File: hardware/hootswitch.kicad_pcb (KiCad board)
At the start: 2 copper layers, 100 x 88 mm, 127 parts, among them J1 Mini-DIN-4-G, J10 POWSEL, J11 TWI, J12 TWI, J2 Mini-DIN-4-G, J3 Mini-DIN-4-G, J4 Mini-DIN-4-G, J5 Mini-DIN-4-G, J6 Mini-DIN-4-G, J7 Barrel_Jack_MountingPin, J8 EXT_POW, J9 SW1, Q1 MMBT3904, Q10 MMBT3904, Q11 MMBT3904, Q12 MMBT3904, Q13 MMBT3904, Q14 MMBT3904, Q15 MMBT3904, Q16 MMBT3904, Q2 MMBT3904, Q3 MMBT3904, Q4 MMBT3904, Q5 MMBT3904, Q6 MMBT3904, Q7 MMBT3904, Q8 MMBT3904, Q9 MMBT3904, SW1 Switch1, U1 PicoW, U10 LTV-357T, U11 LTV-357T, U2 LM1117-5.0, U3 ADuM1201AR, U4 ADuM1201AR, U5 ADuM1201AR, U6 ADuM1201AR, U7 ADuM1201AR, U8 LTV-357T, U9 LTV-357T

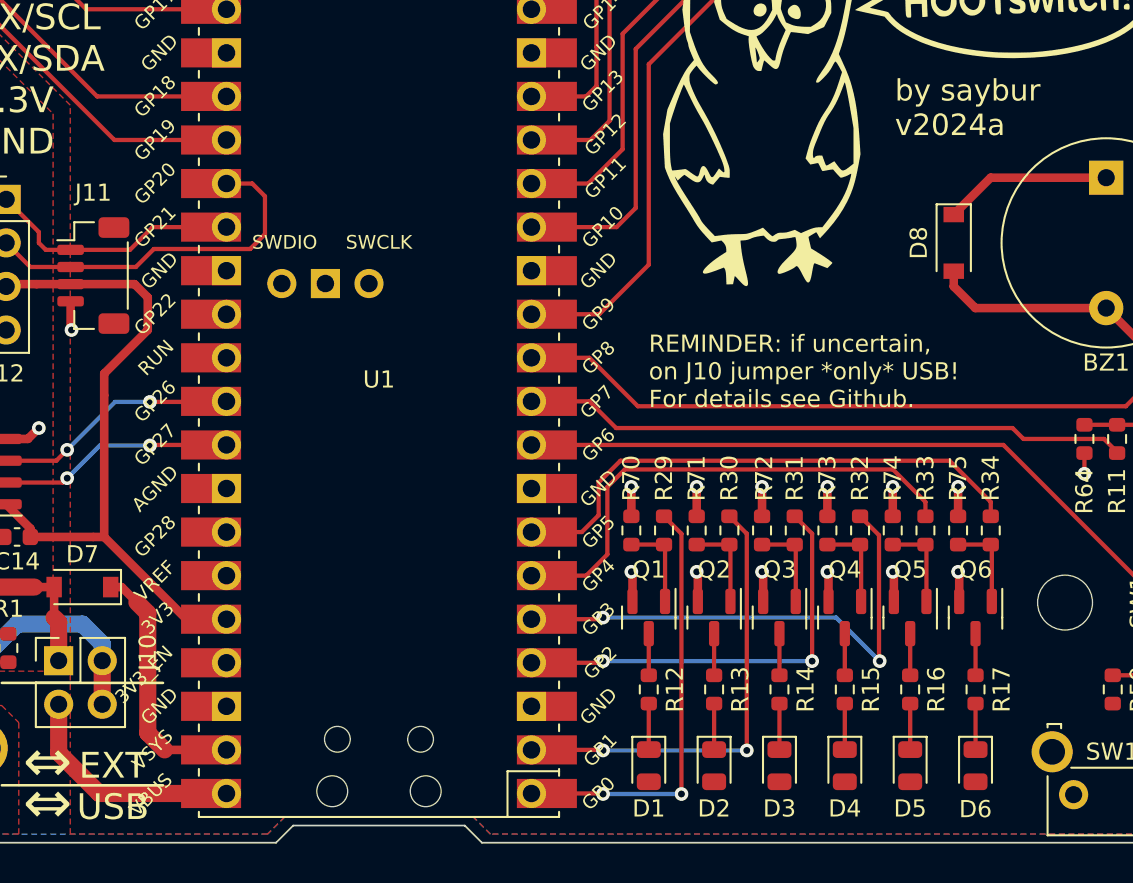
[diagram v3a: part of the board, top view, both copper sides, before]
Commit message: Minor adjustments to silkscreen labels.
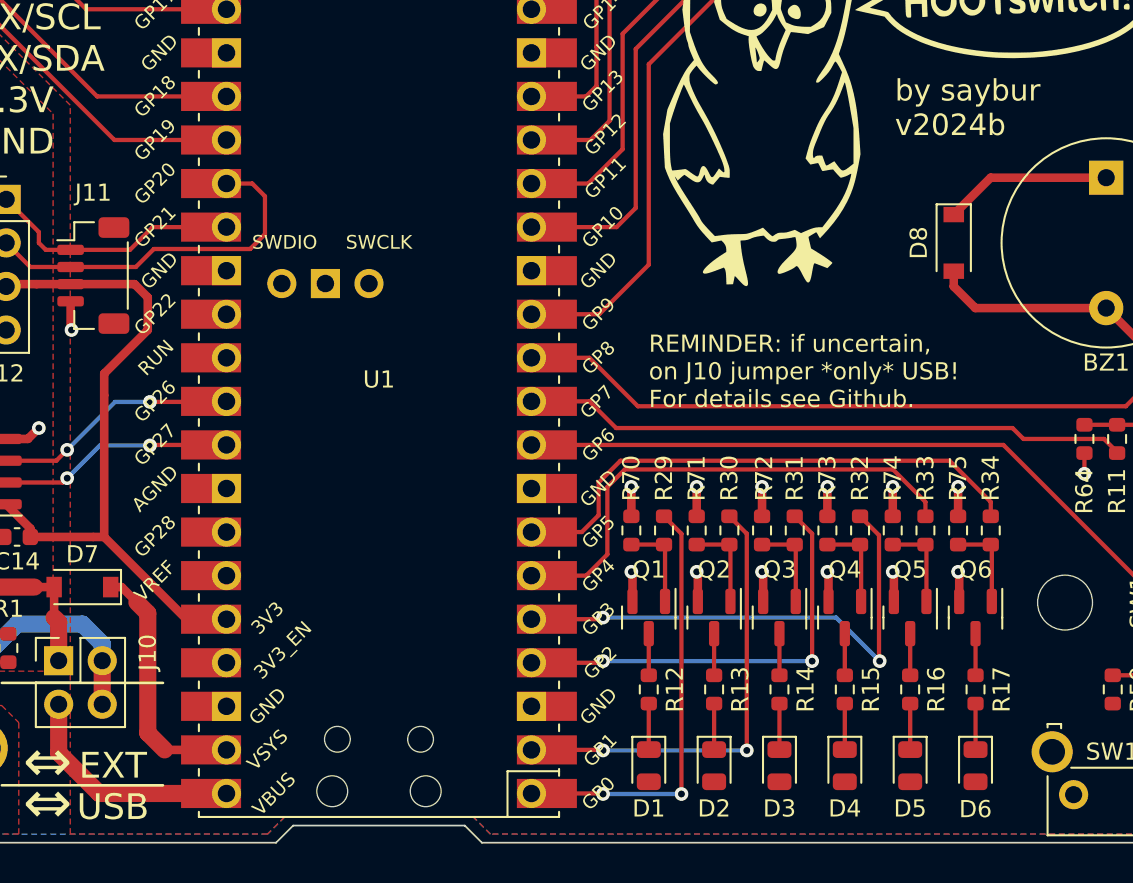
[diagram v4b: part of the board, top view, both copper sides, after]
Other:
- board text added: "by saybur v2024b"
- board text removed: "by saybur v2024a"
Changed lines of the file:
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@@
       (effects (font (size 0.8 0.8) (thickness 0.15)))
     )
-    (fp_text user "VSYS" (at 13.2 -21.59 45) (layer "F.SilkS")
+    (fp_text user "VSYS" (at 6.495 -21.59 45) (layer "F.SilkS")
       (effects (font (size 0.8 0.8) (thickness 0.15)))
     )
@@
       (effects (font (size 0.8 0.8) (thickness 0.15)))
     )
-    (fp_text user "GND" (at 12.8 -19.05 45) (layer "F.SilkS")
+    (fp_text user "GND" (at 6.495 -19.05 45) (layer "F.SilkS")
       (effects (font (size 0.8 0.8) (thickness 0.15)))
     )
@@
       (effects (font (size 0.8 0.8) (thickness 0.15)))
     )
-    (fp_text user "VBUS" (at 13.3 -24.2 45) (layer "F.SilkS")
+    (fp_text user "VBUS" (at 6.114 -24.161 45) (layer "F.SilkS")
       (effects (font (size 0.8 0.8) (thickness 0.15)))
     )
@@
       (effects (font (size 0.8 0.8) (thickness 0.15)))
     )
-    (fp_text user "3V3" (at 12.9 -13.9 45) (layer "F.SilkS")
+    (fp_text user "3V3" (at 6.495 -13.9 45) (layer "F.SilkS")
       (effects (font (size 0.8 0.8) (thickness 0.15)))
     )
@@
       (effects (font (size 0.8 0.8) (thickness 0.15)))
     )
-    (fp_text user "3V3_EN" (at 13.7 -17.2 45) (layer "F.SilkS")
+    (fp_text user "3V3_EN" (at 5.606 -15.779 45) (layer "F.SilkS")
       (effects (font (size 0.8 0.8) (thickness 0.15)))
     )
@@
     (effects (font (size 1 1) (thickness 0.15)))
   )
-  (gr_text "by saybur\nv2024a" (at 140.081 105.156) (layer "F.SilkS")
+  (gr_text "by saybur\nv2024b" (at 140.081 105.156) (layer "F.SilkS")
     (effects (font (size 1.25 1.25) (thickness 0.25)) (justify left))
   )

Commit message: Hardware 2024c.
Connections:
- J7 pad 2: Net-(J7-Pad2) -> GND
- J8 pad 2: Net-(J7-Pad2) -> GND
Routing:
- net GND: track 90.8 -> 100.9 mm
- net Net-(J7-Pad2): track 10.2 -> 0.00 mm
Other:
- board text added: "by saybur v2024c"
- board text removed: "by saybur v2024b"
